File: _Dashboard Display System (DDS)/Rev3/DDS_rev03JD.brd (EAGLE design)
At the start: 71.1 x 73.7 mm, 81 parts, among them J1 36638NEW, Q1 BSS123, Q2 BSS123, U1 PIC18F45K22, U10 DMG6602SVTQ, U11 NCV7805BDTRKG, U12 NCV7805BDTRKG, U13 MAX6818, U2 SN75HVD08DRSOIC, U3 OPA344, U4 NCP1117DT_3.3, U5 DMG6602SVTQ, U6 DMG6602SVTQ, U7 DMG6602SVTQ, U8 DMG6602SVTQ, U9 DMG6602SVTQ

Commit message: DDS ripup
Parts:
- moved C10 53.7 mm to (4.52, 52.7)
- moved D7 15.5 mm to (4.50, 36.6)
- moved R20 14.7 mm to (4.65, 32.5)
- moved R10 14.5 mm to (6.83, 32.1)
- moved D9 14.2 mm to (7.04, 35.5)
- moved U2 3.49 mm to (5.38, 25.7), turned to 180 degrees
- moved U$2 1.68 mm to (9.88, 53.8)
- moved C11 1.07 mm to (7.25, 49.3)
- moved D4 0.76 mm to (63.9, 65.4)
- moved R22 0.71 mm to (67.6, 65.4)
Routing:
- net TX1: track 62.4 -> 0.20 mm
- net RX1: track 59.3 -> 0.00 mm, vias 2 -> 0
- net U2-RE/DE: track 56.0 -> 0.00 mm
- net RS-B: track 39.4 -> 0.00 mm, vias 1 -> 0
- net RS-A: track 36.3 -> 0.00 mm, vias 1 -> 0
- net +5V: track 315.9 -> 284.0 mm
- net TX2: track 90.8 -> 77.7 mm, vias 6 -> 5
- net RX2: track 81.7 -> 72.5 mm, vias 2 -> 1
- net +3V3: track 108.0 -> 112.7 mm
- net N$12: track 39.6 -> 41.3 mm
- net N$9: track 2.52 -> 4.20 mm
- net N$8: track 3.65 -> 5.33 mm
- net N$10: track 3.51 -> 5.19 mm
- net N$17: track 1.67 -> 0.00 mm
- net N$3: track 36.7 -> 38.3 mm
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
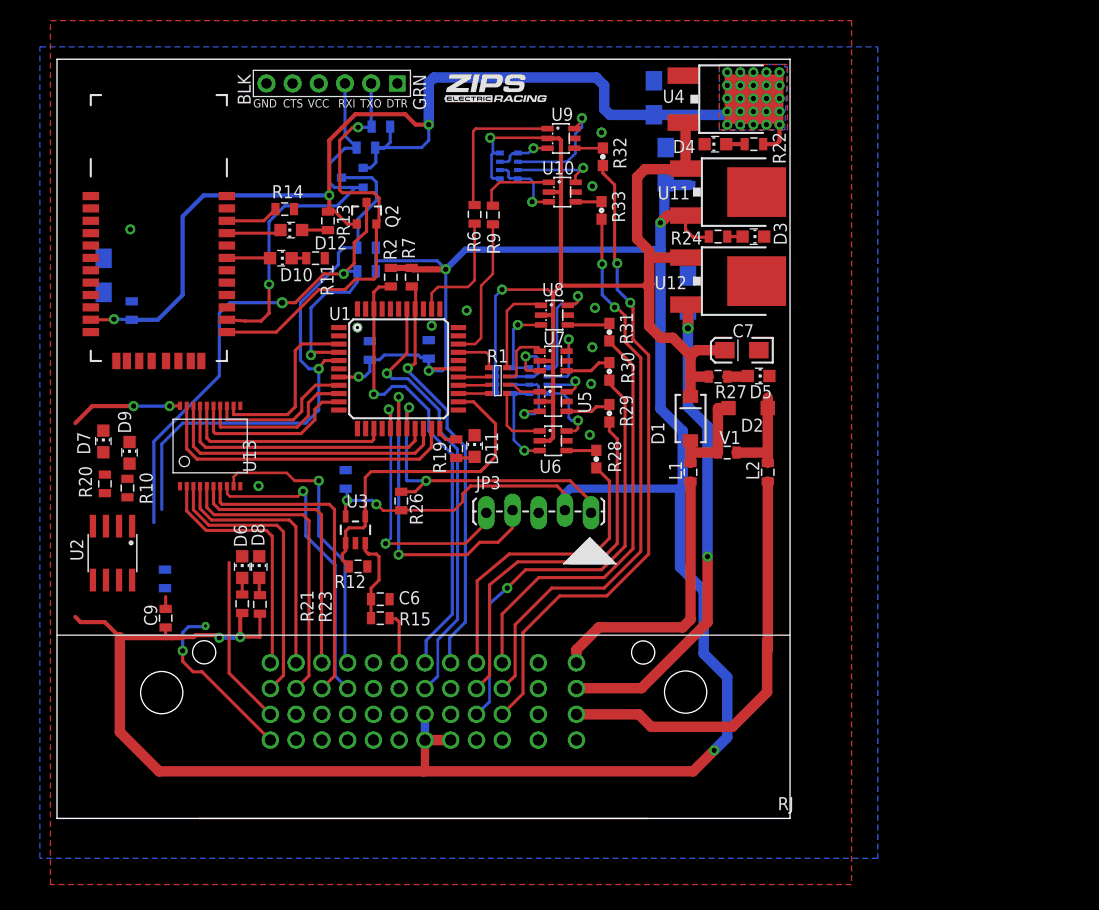
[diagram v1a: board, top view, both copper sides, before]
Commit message: Adding traces and  parts
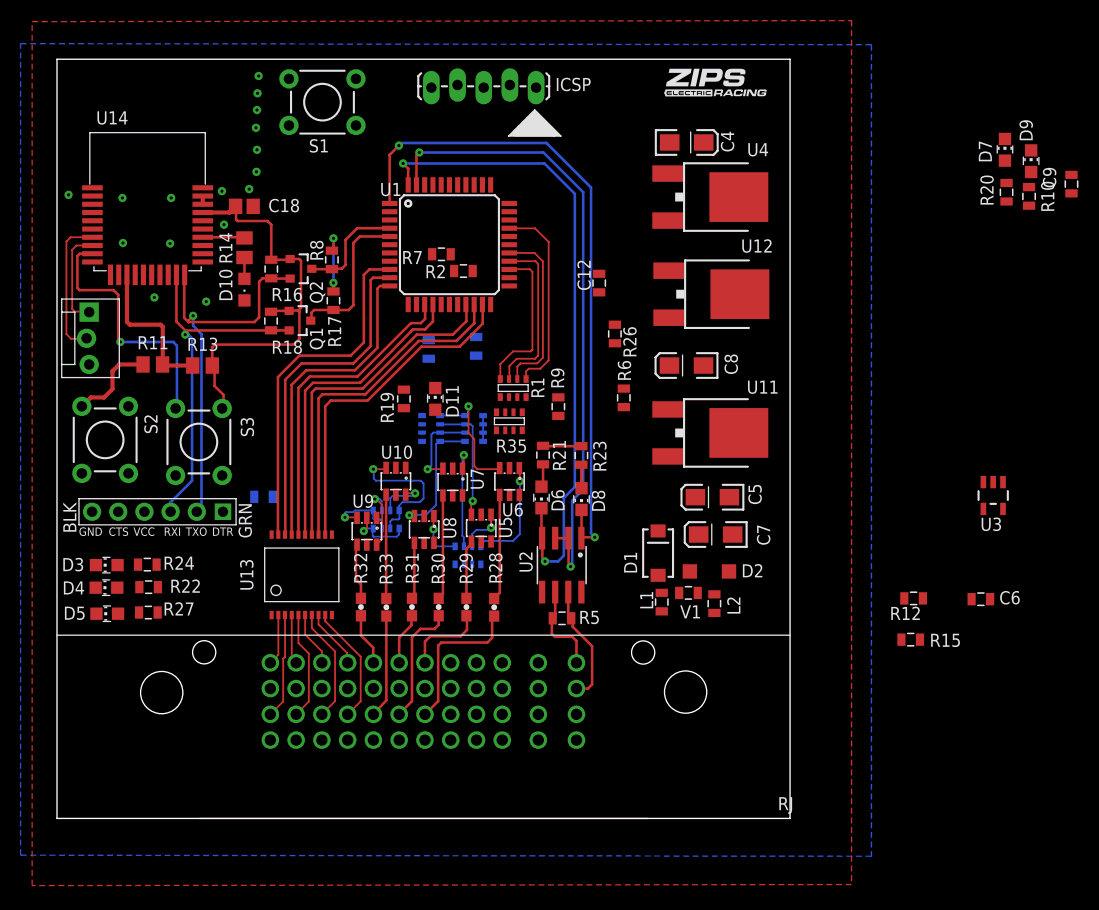
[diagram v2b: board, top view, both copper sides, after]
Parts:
- removed C10: 10UF, FSAE Electric:EIA3216-16V
- removed C11: \0.1UF, FSAE Electric:0805
- removed D12: YELLOW, FSAE Electric:CHIP_LED0805
- removed JP3: (no value), SparkFun-Connectors:1X05_LOCK_LONGPADS
- removed U$2: BLUETOOTH-RN41", SparkFun-RF:RN41
- added C18: 0.1uF, adafruit:C0805
- added ICSP: (no value), SparkFun-Connectors:1X05_LOCK_LONGPADS
- added JP1: (no value), SparkFun-Connectors:MOLEX-1X3_LOCK
- added R34, R35: 10K, FSAE Electric:MNR14
- added S1: SWITCH-MOMENTARY-2PTH, SparkFun-Electromechanical:TACTILE-PTH
- added S2: NO, SparkFun-Electromechanical:TACTILE-PTH
- added S3: (no value), SparkFun-Electromechanical:TACTILE-PTH
- added U14: A20737AGM, RJC:A20737AGM
- D10: value AMBER -> (none); device FSAE Electric:CHIP_LED0805 -> adafruit:CHIPLED_0805
- R11: value 330 -> 1K; device FSAE Electric:0805 -> adafruit:M0805
- R13: value 330 -> 10K; device FSAE Electric:0805 -> adafruit:M0805
- R14: value 100K -> 1K; device FSAE Electric:0805 -> adafruit:M0805
- R25, R3: value RN-4_10K -> 10K
- R28, R29, R30, R31, R32, R33: value RESPLACEHOLDER -> (none)
- moved C9 97.5 mm to (98.4, 61.5)
- moved D9 91.9 mm to (94.5, 63.8)
- moved D7 91.9 mm to (92.0, 64.9)
- moved R10 91.9 mm to (94.3, 60.4)
- moved R20 91.9 mm to (92.1, 60.8)
- moved D4 73.1 mm to (4.80, 22.4)
- moved R22 72.8 mm to (8.89, 22.4)
- moved D3 70.4 mm to (4.83, 24.6), turned to 90 degrees
- moved D5 67.3 mm to (4.88, 19.9), turned to 90 degrees
- moved R24 63.9 mm to (8.76, 24.6), turned to 0 degrees
- moved U3 62.0 mm to (90.8, 31.3), turned to 180 degrees
- moved R27 59.8 mm to (8.86, 20.0), turned to 0 degrees
- moved C6 58.3 mm to (89.6, 21.3)
- moved R12 54.0 mm to (83.1, 21.3)
- moved R15 51.5 mm to (82.8, 17.3)
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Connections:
- net B1 renamed N$4
- net BSAVE renamed N$48
- net O5 renamed S_IN_5
- net START renamed N$50
- removed net B2: J1.2, U13.3
- removed net BREAK: J1.6, U13.5
- removed net N$10: R14.2, U$2.22
- removed net N$12: JP19.P$2, Q2.2, R16.1, U$2.13
- removed net N$13: D10.C, R11.2
- removed net N$3: JP19.P$3, Q1.2, R18.1, U$2.14
- removed net N$4 (its old number): J1.10, U13.7
- removed net N$8: D12.C, U$2.21
- removed net N$9: D10.A, U$2.19
- removed net O1: U1.3, U13.12
- removed net O2: U1.8, U13.13
- removed net O3: U1.9, U13.14
- removed net O4: U1.10, U13.15
- removed net O6: U1.19, U13.17
- removed net O7: U1.20, U13.18
- removed net O8: U1.21, U13.19
- new net BLE-INT: U14.23
- new net BLE-RX: JP19.P$2, Q2.2, R16.1, U14.20
- new net BLE-TX: JP19.P$3, Q1.2, R18.1, U14.19
- new net BLE_RESET: R11.2, R13.1, U14.13
- new net N$47: J1.3, U13.3
- new net N$49: J1.7, U13.5
- new net N$51: J1.11, U13.7
- new net N$52: U14.28, U14.29
- new net N$54: R11.1, S2.3
- new net N$57: D10.A, R14.1
- new net N$58: JP1.1, U14.8
- new net N$60: JP1.2, U14.7
- new net N$61: S3.3, U14.9
- new net S_IN_1: U1.21, U13.12
- new net S_IN_2: U1.20, U13.13
- new net S_IN_3: U1.19, U13.14
- new net S_IN_4: U1.15, U13.15
- new net S_IN_6: U1.11, U13.17
- new net S_IN_7: U1.10, U13.18
- new net S_IN_8: U1.9, U13.19
- net +: now also J1.47; no longer J1.45
- net +3V3: now also C18.1, S3.1, U14.27; no longer C10.A, C11.1, U$2.11
- net +5V: now also ICSP.2; no longer J1.27, J1.28, J1.32, JP3.2
- net -: no longer J1.47
- net 5V2: no longer J1.46
- net ACK: now also J1.15; no longer J1.13
- net GND: now also C18.2, D10.C, ICSP.3, J1.10, J1.14, J1.2, J1.26, J1.28, J1.4, J1.6, J1.8, JP1.3, R34.1, R34.2, R34.3, R34.4, R35.1, R35.2, S1.1, S2.1, U14.1, U14.11, U14.3, U14.30, U14.6; no longer C10.C, C11.2, J1.11, J1.15, J1.17, J1.19, J1.23, J1.40, J1.41, J1.42, J1.43, J1.44, J1.48, JP3.3, R11.1, R14.1, U$2.1, U$2.12, U$2.28, U$2.29
- net N$23: now also R34.8
- net N$24: no longer J1.21
- net N$29: now also R34.7
- net N$40: now also ICSP.4; no longer JP3.4
- net N$41: now also R34.6
- net N$42: now also R34.5
- net N$43: now also ICSP.5; no longer JP3.5
- net N$44: now also R35.8
- net N$45: now also R35.7
- net N$46: now also ICSP.1, S1.3; no longer JP3.1
- net N$6: now also R14.2, U14.24; no longer D12.A, R13.1
- net POS-SWITCH: no longer J1.26
- net RS-A: now also J1.45; no longer J1.7
- net RS-B: now also J1.46; no longer J1.8
- net RX2: no longer J1.3
- net SCL: no longer J1.29
- net SDA: no longer J1.25
- net TALK: now also J1.13; no longer J1.14
- net TX2: no longer J1.4
- net _OLED0: now also J1.17; no longer J1.39
- net _OLED1: now also J1.19; no longer J1.38
- net _OLED2: now also J1.21; no longer J1.37
- net _OLED3: now also J1.23; no longer J1.35
- net _OLED4: now also J1.25; no longer J1.34
- net _OLED5: now also J1.27; no longer J1.33
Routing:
- net +5V: track 284.0 -> 10.2 mm, vias 11 -> 2
- net +9V: track 117.0 -> 8.92 mm, vias 2 -> 1
- net +3V3: track 112.7 -> 40.4 mm, vias 28 -> 0
- net TX2: track 77.7 -> 10.6 mm, vias 5 -> 0
- net RX1: track 0.00 -> 65.9 mm, vias 0 -> 2
- net TX1: track 0.20 -> 63.1 mm, vias 0 -> 2
- net U2-RE/DE: track 0.00 -> 61.8 mm, vias 0 -> 2
- net _OLED0: track 63.7 -> 5.06 mm, vias 2 -> 0
- net RX2: track 72.5 -> 15.0 mm, vias 1 -> 0
- net 5V2: track 51.2 -> 0.00 mm, vias 2 -> 0
- net _OLED1: track 55.8 -> 10.0 mm, vias 2 -> 0
- net SDA: track 44.9 -> 0.10 mm, vias 1 -> 0
- net POS-SWITCH: track 42.7 -> 0.00 mm, vias 1 -> 0
- net -: track 41.8 -> 0.00 mm
- net N$12: track 41.3 -> 0.00 mm, vias 1 -> 0
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- removed copper zone on layer 1, net +3V3
- removed copper zone on layer 16, net +3V3

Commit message: 
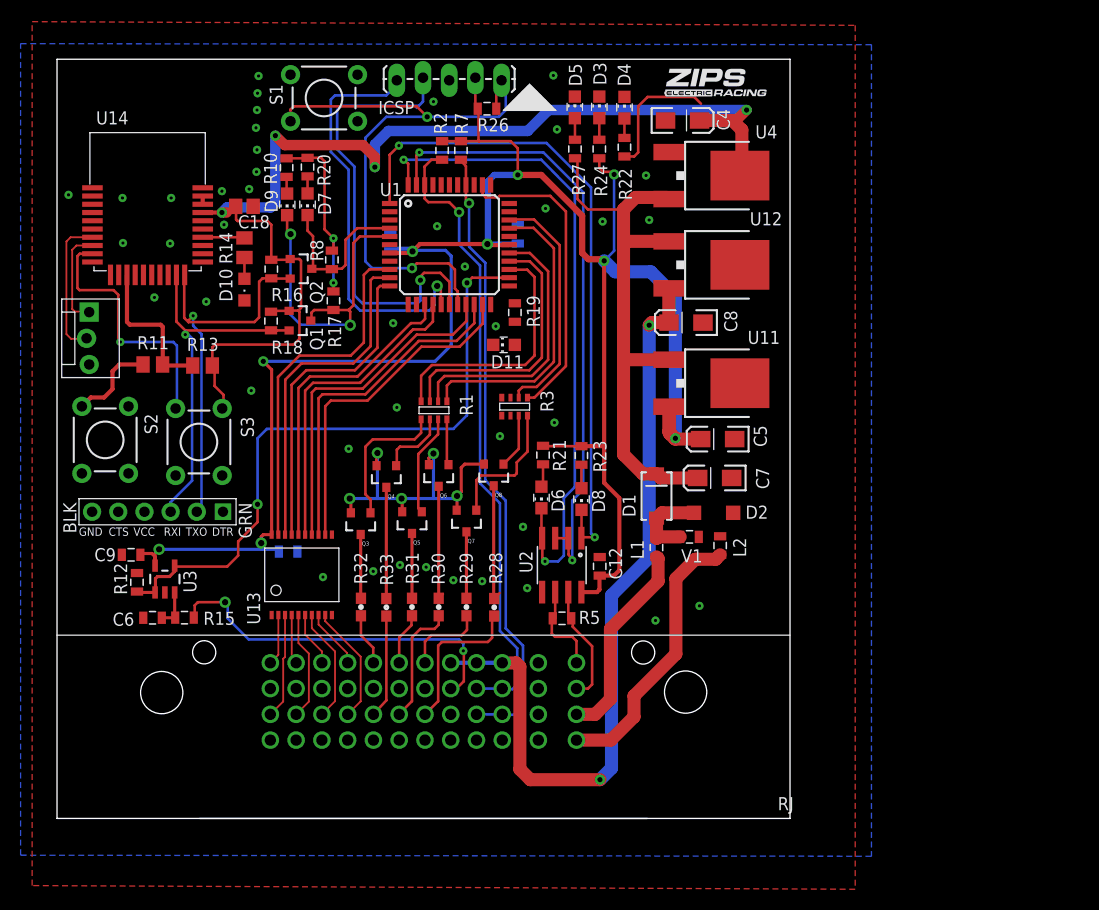
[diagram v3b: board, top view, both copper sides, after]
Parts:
- removed R25, R34, R35, R4: 10K, FSAE Electric:MNR14
- removed R6, R9: 1K, FSAE Electric:0805
- removed U10, U5, U6, U7, U8, U9: DMG6602SVTQ, FSAE Electric:SOT23-6
- added Q3, Q4, Q5, Q6, Q7, Q8: PNP_MMBT4403LT3G, FSAE Electric:SOT23
- R1: value 1K -> RN-4_2.2K
- R28, R29, R30, R31, R32, R33: value (none) -> RESPLACEHOLDER
- R3: value 10K -> RN-4_2.2K
- moved C9 98.1 mm to (7.19, 25.6), turned to 180 degrees
- moved U3 80.8 mm to (10.5, 23.2), turned to 0 degrees
- moved C6 80.4 mm to (9.27, 19.5), turned to 180 degrees
- moved R12 75.4 mm to (7.76, 22.9), turned to 270 degrees
- moved D9 72.3 mm to (22.3, 59.6), turned to 180 degrees
- moved R10 72.1 mm to (22.3, 63.1), turned to 90 degrees
- moved R15 70.5 mm to (12.4, 19.5)
- moved D4 68.5 mm to (55.1, 69.0), turned to 0 degrees
- moved D7 67.9 mm to (24.3, 59.6), turned to 180 degrees
- moved R20 67.9 mm to (24.3, 63.2), turned to 90 degrees
- moved D5 66.9 mm to (50.2, 69.0), turned to 0 degrees
- moved D3 65.2 mm to (52.6, 69.0), turned to 0 degrees
- moved R22 62.9 mm to (55.1, 65.1), turned to 270 degrees
- moved R27 61.1 mm to (50.3, 64.9), turned to 270 degrees
- moved R24 59.6 mm to (52.6, 64.9), turned to 270 degrees
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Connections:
- removed net N$16: R25.1, R3.8, U6.3
- removed net N$21: R25.7, U5.6
- removed net N$22: R25.2, R3.7, U5.3
- removed net N$23: R1.5, R34.8, U6.1
- removed net N$24: R15.2
- removed net N$27: R25.6, U7.6
- removed net N$28: R25.3, R3.6, U7.3
- removed net N$29: R1.6, R34.7, U5.1
- removed net N$30: R25.5, U8.6
- removed net N$31: R25.4, R3.5, U8.3
- removed net N$33: R4.1, R4.7, U9.3
- removed net N$34: R4.2, U9.6
- removed net N$36: R4.3, U10.6
- removed net N$37: R4.4, R4.6, U10.3
- removed net N$41: R1.7, R34.6, U7.1
- removed net N$42: R1.8, R34.5, U8.1
- removed net N$44: R35.8, R6.2, U9.1
- removed net N$45: R35.7, R9.2, U10.1
- new net N$10: Q5.1, R1.7
- new net N$12: Q7.1, R3.8
- new net N$13: Q8.1, R3.7
- new net N$3: J1.30, R15.2
- new net N$8: Q6.1, R1.8
- new net N$9: Q4.1, R1.6
- net +9V: now also Q3.2, Q4.2, Q5.2, Q6.2, Q7.2, Q8.2; no longer R3.1, R3.2, R3.3, R3.4, R4.5, R4.8, U10.2, U5.2, U6.2, U7.2, U8.2, U9.2
- net -: now also J1.48
- net 5V2: now also J1.29, J1.33, J1.37
- net GND: now also J1.32, J1.36, J1.40; no longer R34.1, R34.2, R34.3, R34.4, R35.1, R35.2, U10.5, U5.5, U6.5, U7.5, U8.5, U9.5
- net LED0: now also R3.1; no longer R6.1
- net LED1: now also R3.2; no longer R9.1
- net N$20: now also Q7.3; no longer U5.4
- net N$32: now also Q6.3; no longer U7.4
- net N$35: now also Q5.3; no longer U8.4
- net N$38: now also Q3.3; no longer U9.4
- net N$39: now also Q4.3; no longer U10.4
- net N$5: now also Q8.3; no longer U6.4
- net N$7: now also Q3.1, R1.5; no longer R25.8, U6.6
- net SCL: now also J1.35, J1.39
- net SDA: now also J1.34, J1.38
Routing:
- net +5V: track 10.2 -> 226.6 mm, vias 2 -> 11
- net +3V3: track 40.4 -> 130.3 mm, vias 0 -> 4
- net +9V: track 8.92 -> 86.0 mm, vias 1 -> 5
- net 5V2: track 0.00 -> 76.4 mm, vias 0 -> 2
- net VOL: track 0.00 -> 63.1 mm, vias 0 -> 2
- net SDA: track 0.10 -> 61.9 mm, vias 0 -> 1
- net N$46: track 0.00 -> 60.6 mm, vias 0 -> 2
- net SCL: track 0.00 -> 60.4 mm, vias 0 -> 1
- net N$40: track 0.00 -> 44.6 mm, vias 0 -> 1
- net N$43: track 0.00 -> 40.5 mm, vias 0 -> 1
- net N$3: track 0.00 -> 35.1 mm, vias 0 -> 2
- net LED0: track 0.00 -> 29.9 mm
- net -: track 0.00 -> 26.9 mm
- net LED1: track 0.00 -> 23.2 mm
- net +: track 0.00 -> 19.7 mm
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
